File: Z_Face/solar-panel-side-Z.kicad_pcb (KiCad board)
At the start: 4 copper layers, 100 x 100 mm, 32 parts, among them J1 CON-5040500591, J2 Face0, J3 Face1, J4 Conn_01x01, J5 Conn_01x01, J6 Conn_01x01, J7 Conn_01x01, J8 Face2, J9 Face3, U1 VEML7700, U2 DRV2605LDGS, U3 MCP9808_DFN

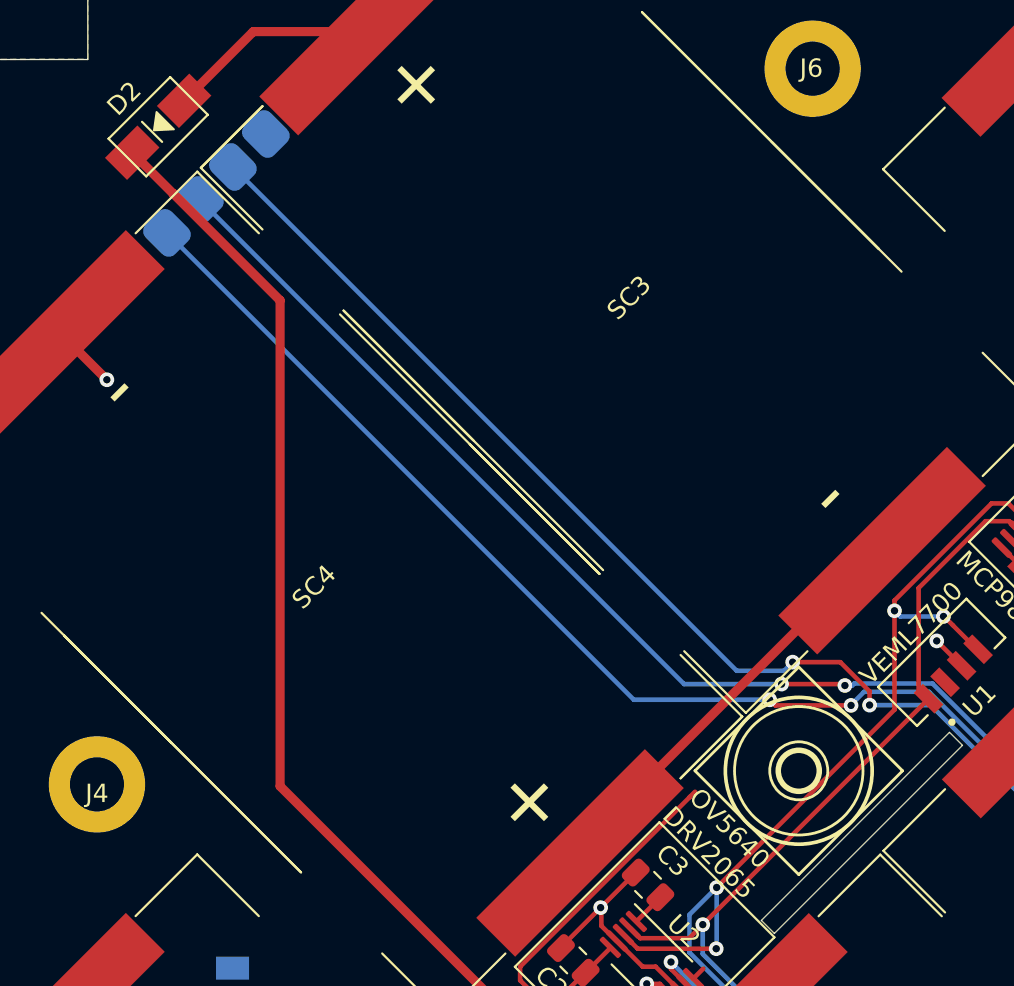
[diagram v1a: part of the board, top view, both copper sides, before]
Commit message: Squashed commit of the following:
commit e254adcde77272bf9c297392939bbb8f65e8d1c6
Author: Michael Pham <61564344+Mikefly123@users.noreply.github.com>
Date:   Tue May 28 21:23:36 2024 -0700

    Fixed Antenna Board

commit 045481aa1d64479ef8ca8c2eedf132e30a3c2c12
Author: Michael Pham <61564344+Mikefly123@users.noreply.github.com>
Date:   Tue May 28 20:29:56 2024 -0700

    Consolidating files

commit 0d9b312b1d72281e33c094203cb00ac56d2c935d
Author: kdizzlle <112121179+kdizzlle@users.noreply.github.com>
Date:   Tue May 28 13:55:35 2024 -0700

    added extra pin to z face

    moved it slightly closer also
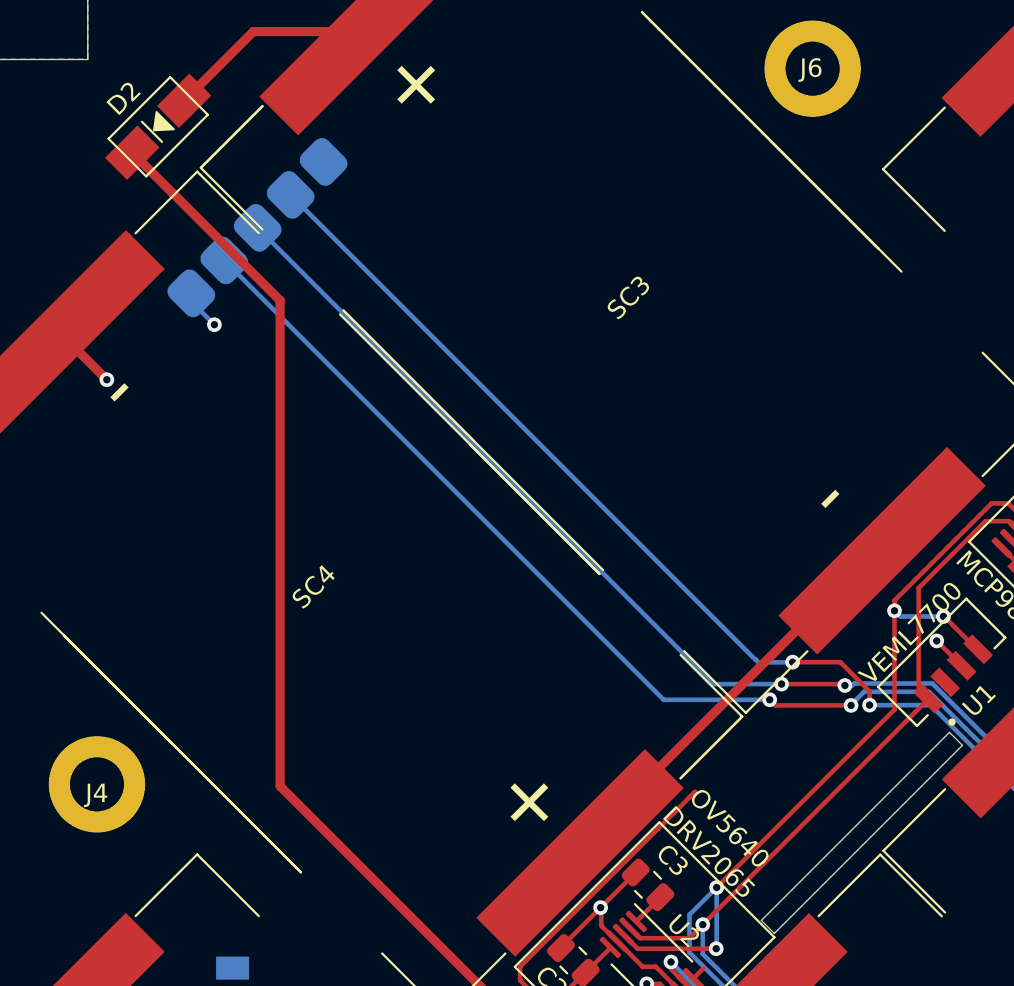
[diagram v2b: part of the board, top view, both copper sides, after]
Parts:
- removed ?: , clipboard:b0880f64-8dff-43fb-af48-c7da55ca08b3
- moved U5 3.32 mm to (115.8, 51.2)
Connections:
- U5 pad 5: (no net) -> +3V3
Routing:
- net Camera_Pwr: track 95.0 -> 90.9 mm
- net Camera_SDA: track 101.9 -> 98.1 mm
- net Camera_SCL: track 100.2 -> 96.5 mm
- net +3V3: track 39.0 -> 41.4 mm, vias 2 -> 3
